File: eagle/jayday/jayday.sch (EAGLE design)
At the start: 35 parts, among them IC1 TPS2115, X1 2X5_1.27MM, X17 DX2R005HN2E700

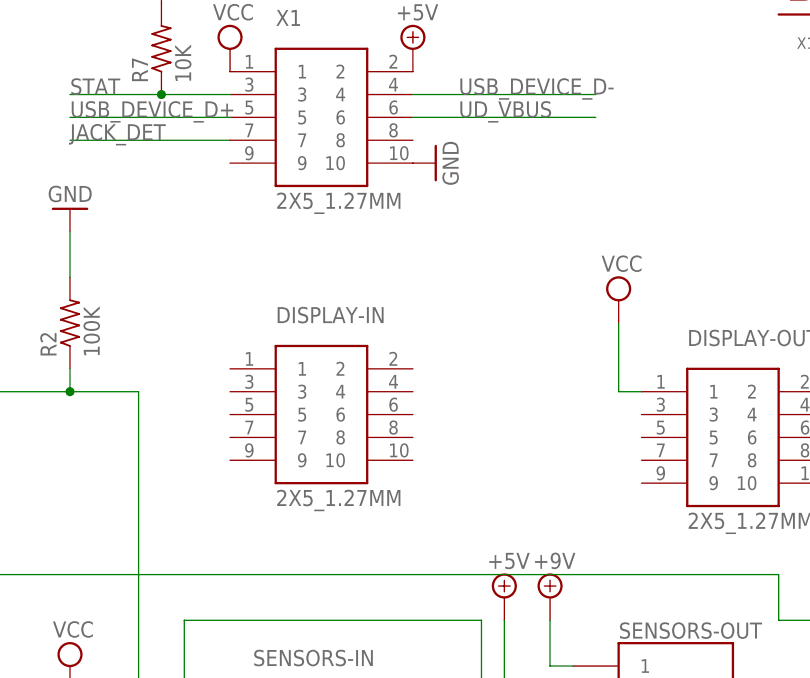
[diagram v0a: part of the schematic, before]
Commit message: added board with sim900
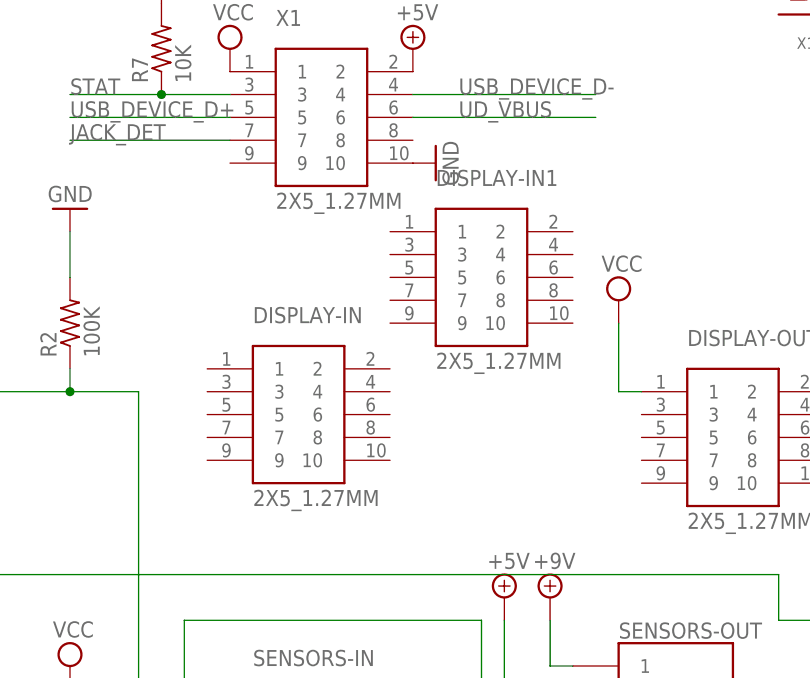
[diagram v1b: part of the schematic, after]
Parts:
- added DISPLAY-IN1: 2X5_1.27MM, GHI:2X5_1.27MM
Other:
- moved on the sheet: DISPLAY-IN
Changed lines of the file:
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@@
 <part name="PWR2" library="led" deviceset="LED" device="CHIPLED_0805"/>
 <part name="R10" library="rcl" deviceset="R-US_" device="R0603" value="1K"/>
+<part name="DISPLAY-IN1" library="GHI" deviceset="2X5_1.27MM" device=""/>
 </parts>
 <sheets>
@@
 <instance part="FETS-X-Y" gate="G$1" x="-48.26" y="119.38"/>
 <instance part="SENSORS-IN" gate="G$1" x="5.08" y="81.28"/>
-<instance part="DISPLAY-IN" gate="G$1" x="7.62" y="119.38"/>
+<instance part="DISPLAY-IN" gate="G$1" x="5.08" y="119.38"/>
 <instance part="DISPLAY-OUT" gate="G$1" x="53.34" y="116.84"/>
 <instance part="GND6" gate="1" x="68.58" y="66.04"/>
@@
 <instance part="PWR2" gate="G$1" x="38.1" y="38.1"/>
 <instance part="R10" gate="G$1" x="38.1" y="50.8" rot="R90"/>
+<instance part="DISPLAY-IN1" gate="G$1" x="25.4" y="134.62"/>
 </instances>
 <busses>
